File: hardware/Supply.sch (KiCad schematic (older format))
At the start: 11 parts, among them IC8 TL7702B, J1 Power, SW1 RESET, U1 R-785.0-0.5

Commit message: Working on layout
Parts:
- added D13: POWER, LED_THT:LED_D5.0mm, symbol Device:LED
- added R8: 470, Resistor_THT:R_Axial_DIN0207_L6.3mm_D2.5mm_P7.62mm_Horizontal, symbol Device:R
- C10, C11, C12, C13: footprint Capacitor_THT:C_Rect_L4.6mm_W2.0mm_P2.50mm_MKS02_FKP02 -> Capacitor_THT:C_Rect_L4.0mm_W2.5mm_P2.50mm; Mfr. AVX -> TDK; Mfr. No. SR295E104MAATR2 -> FA18X8R1H104KRU06; Mouser 581-SR295E104MAATR2 -> 810-FA18X8R1H104KRU6
- IC8: value TL7702B -> TL7702
- J1: value Power -> 12V
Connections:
- wire segments 33 -> 38
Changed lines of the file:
@@
 EESchema Schematic File Version 4
-LIBS:Sweet 6502 Computer-cache
+LIBS:Retro PC-cache
 EELAYER 30 0
 EELAYER END
@@
 F 1 "10k" H 5720 3605 50  0000 L CNN
 F 2 "Resistor_THT:R_Axial_DIN0207_L6.3mm_D2.5mm_P7.62mm_Horizontal" V 5580 3650 50  0001 C CNN
-F 3 "~" H 5650 3650 50  0001 C CNN
+F 3 "https://www.mouser.de/datasheet/2/427/sfr16s25-239894.pdf" H 5650 3650 50  0001 C CNN
 F 4 "Vishay / BC Components" H 5650 3650 50  0001 C CNN "Mfr."
 F 5 "SFR25H0001002JR500" H 5650 3650 50  0001 C CNN "Mfr. No."
@@
 F 0 "C11" H 6215 4446 50  0000 L CNN
 F 1 "100nF" H 6215 4355 50  0000 L CNN
-F 2 "Capacitor_THT:C_Rect_L4.6mm_W2.0mm_P2.50mm_MKS02_FKP02" H 6138 4250 50  0001 C CNN
-F 3 "~" H 6100 4400 50  0001 C CNN
-F 4 "AVX" H 6100 4400 50  0001 C CNN "Mfr."
-F 5 "SR295E104MAATR2" H 6100 4400 50  0001 C CNN "Mfr. No."
-F 6 "581-SR295E104MAATR2" H 6100 4400 50  0001 C CNN "Mouser"
+F 2 "Capacitor_THT:C_Rect_L4.0mm_W2.5mm_P2.50mm" H 6138 4250 50  0001 C CNN
+F 3 "https://www.mouser.de/datasheet/2/400/eadmlcc_halogenfree_fa150_en-890480.pdf" H 6100 4400 50  0001 C CNN
+F 4 "TDK" H 6100 4400 50  0001 C CNN "Mfr."
+F 5 "FA18X8R1H104KRU06" H 6100 4400 50  0001 C CNN "Mfr. No."
+F 6 "810-FA18X8R1H104KRU6" H 6100 4400 50  0001 C CNN "Mouser"
 	1    6100 4400
 	1    0    0    -1
@@
 F 1 "330nF" H 3365 4155 50  0000 L CNN
 F 2 "Capacitor_THT:C_Rect_L4.0mm_W2.5mm_P2.50mm" H 3288 4050 50  0001 C CNN
-F 3 "~" H 3250 4200 50  0001 C CNN
+F 3 "https://www.mouser.de/datasheet/2/40/SR-Series-1016911.pdf" H 3250 4200 50  0001 C CNN
 F 4 "AVX" H 3250 4200 50  0001 C CNN "Mfr."
 F 5 "SR205E334MARTR1" H 3250 4200 50  0001 C CNN "Mfr. No."
@@
 F 0 "C10" H 4315 4246 50  0000 L CNN
 F 1 "100nF" H 4315 4155 50  0000 L CNN
-F 2 "Capacitor_THT:C_Rect_L4.6mm_W2.0mm_P2.50mm_MKS02_FKP02" H 4238 4050 50  0001 C CNN
-F 3 "~" H 4200 4200 50  0001 C CNN
-F 4 "AVX" H 4200 4200 50  0001 C CNN "Mfr."
-F 5 "SR295E104MAATR2" H 4200 4200 50  0001 C CNN "Mfr. No."
-F 6 "581-SR295E104MAATR2" H 4200 4200 50  0001 C CNN "Mouser"
+F 2 "Capacitor_THT:C_Rect_L4.0mm_W2.5mm_P2.50mm" H 4238 4050 50  0001 C CNN
+F 3 "https://www.mouser.de/datasheet/2/400/eadmlcc_halogenfree_fa150_en-890480.pdf" H 4200 4200 50  0001 C CNN
+F 4 "TDK" H 4200 4200 50  0001 C CNN "Mfr."
+F 5 "FA18X8R1H104KRU06" H 4200 4200 50  0001 C CNN "Mfr. No."
+F 6 "810-FA18X8R1H104KRU6" H 4200 4200 50  0001 C CNN "Mouser"
 	1    4200 4200
 	1    0    0    -1
@@
 $EndComp
 Wire Wire Line
-	4200 3300 4200 3750
+	4200 3300 4200 3400
 Wire Wire Line
 	3450 3750 3250 3750
@@
 F 1 "1N4148" H 3000 3624 50  0000 C CNN
 F 2 "Diode_THT:D_DO-35_SOD27_P7.62mm_Horizontal" H 3000 3575 50  0001 C CNN
-F 3 "https://www.vishay.com/docs/81857/1n4148.pdf" H 3000 3750 50  0001 C CNN
+F 3 "https://www.mouser.de/datasheet/2/308/1N4148-1118184.pdf" H 3000 3750 50  0001 C CNN
 F 4 "ON Semiconductor / Fairchild" H 3000 3750 50  0001 C CNN "Mfr."
 F 5 "1N4148" H 3000 3750 50  0001 C CNN "Mfr. No."
@@
 AR Path="/5E9728CC/5E9AA4C9" Ref="J1"  Part="1"
 F 0 "J1" H 2457 4175 50  0000 C CNN
-F 1 "Power" H 2457 4084 50  0000 C CNN
+F 1 "12V" H 2457 4084 50  0000 C CNN
 F 2 "Connector_BarrelJack:BarrelJack_Wuerth_6941xx301002" H 2450 3810 50  0001 C CNN
 F 3 "https://katalog.we-online.de/em/datasheet/6941xx301002.pdf" H 2450 3810 50  0001 C CNN
@@
 F 0 "C12" H 6715 4446 50  0000 L CNN
 F 1 "100nF" H 6715 4355 50  0000 L CNN
-F 2 "Capacitor_THT:C_Rect_L4.6mm_W2.0mm_P2.50mm_MKS02_FKP02" H 6638 4250 50  0001 C CNN
-F 3 "~" H 6600 4400 50  0001 C CNN
-F 4 "AVX" H 6600 4400 50  0001 C CNN "Mfr."
-F 5 "SR295E104MAATR2" H 6600 4400 50  0001 C CNN "Mfr. No."
-F 6 "581-SR295E104MAATR2" H 6600 4400 50  0001 C CNN "Mouser"
+F 2 "Capacitor_THT:C_Rect_L4.0mm_W2.5mm_P2.50mm" H 6638 4250 50  0001 C CNN
+F 3 "https://www.mouser.de/datasheet/2/400/eadmlcc_halogenfree_fa150_en-890480.pdf" H 6600 4400 50  0001 C CNN
+F 4 "TDK" H 6600 4400 50  0001 C CNN "Mfr."
+F 5 "FA18X8R1H104KRU06" H 6600 4400 50  0001 C CNN "Mfr. No."
+F 6 "810-FA18X8R1H104KRU6" H 6600 4400 50  0001 C CNN "Mouser"
 	1    6600 4400
 	1    0    0    -1
@@
 F 0 "C13" H 8015 4446 50  0000 L CNN
 F 1 "100nF" H 8015 4355 50  0001 L CNN
-F 2 "Capacitor_THT:C_Rect_L4.6mm_W2.0mm_P2.50mm_MKS02_FKP02" H 7938 4250 50  0001 C CNN
-F 3 "~" H 7900 4400 50  0001 C CNN
-F 4 "AVX" H 7900 4400 50  0001 C CNN "Mfr."
-F 5 "SR295E104MAATR2" H 7900 4400 50  0001 C CNN "Mfr. No."
-F 6 "581-SR295E104MAATR2" H 7900 4400 50  0001 C CNN "Mouser"
+F 2 "Capacitor_THT:C_Rect_L4.0mm_W2.5mm_P2.50mm" H 7938 4250 50  0001 C CNN
+F 3 "https://www.mouser.de/datasheet/2/400/eadmlcc_halogenfree_fa150_en-890480.pdf" H 7900 4400 50  0001 C CNN
+F 4 "TDK" H 7900 4400 50  0001 C CNN "Mfr."
+F 5 "FA18X8R1H104KRU06" H 7900 4400 50  0001 C CNN "Mfr. No."
+F 6 "810-FA18X8R1H104KRU6" H 7900 4400 50  0001 C CNN "Mouser"
 	1    7900 4400
 	1    0    0    -1
@@
 AR Path="/5E9728CC/5E9AA51D" Ref="IC8"  Part="1"
 F 0 "IC8" H 6950 4350 50  0000 C CNN
-F 1 "TL7702B" H 7050 3650 50  0000 C CNN
+F 1 "TL7702" H 7050 3650 50  0000 C CNN
 F 2 "Package_DIP:DIP-8_W7.62mm_LongPads" H 7300 4000 50  0001 C CNN
 F 3 "http://www.ti.com.cn/cn/lit/ds/symlink/tl7705b.pdf" H 7300 4000 50  0001 C CNN
@@
 Wire Wire Line
 	2750 3950 2750 4650
+$Comp
+L Device:LED D?
+U 1 1 5D9EA3B0
+P 4750 4350
+AR Path="/5D9EA3B0" Ref="D?"  Part="1"
+AR Path="/5EB09E21/5D9EA3B0" Ref="D?"  Part="1"
+AR Path="/5EC67F7B/5D9EA3B0" Ref="D?"  Part="1"
+AR Path="/5E9728CC/5D9EA3B0" Ref="D13"  Part="1"
+F 0 "D13" V 4800 4200 50  0000 R CNN
+F 1 "POWER" V 4700 4200 50  0000 R CNN
+F 2 "LED_THT:LED_D5.0mm" H 4750 4350 50  0001 C CNN
+F 3 "https://www.mouser.de/datasheet/2/90/C503B_RAS_RAN_AAS_AAN_RBS_RBN_ABS_ABN_RCS_RCN_ACS_-269115.pdf" H 4750 4350 50  0001 C CNN
+F 4 "Cree Inc." H 4750 4350 50  0001 C CNN "Mfr."
+F 5 "C503B-RAN-CZ0C0AA1" H 4750 4350 50  0001 C CNN "Mfr. No."
+F 6 "941-C503BRANCZ0C0AA1" H 4750 4350 50  0001 C CNN "Mouser"
+	1    4750 4350
+	0    -1   -1   0
+$EndComp
+$Comp
+L Device:R R?
+U 1 1 5D9EA844
+P 4750 3850
+AR Path="/5D9EA844" Ref="R?"  Part="1"
+AR Path="/5E9728CC/5D9EA844" Ref="R8"  Part="1"
+F 0 "R8" H 4820 3896 50  0000 L CNN
+F 1 "470" H 4820 3805 50  0000 L CNN
+F 2 "Resistor_THT:R_Axial_DIN0207_L6.3mm_D2.5mm_P7.62mm_Horizontal" V 4680 3850 50  0001 C CNN
+F 3 "" H 4750 3850 50  0001 C CNN
+	1    4750 3850
+	1    0    0    -1
+$EndComp
+Wire Wire Line
+	4200 3400 4750 3400
+Wire Wire Line
+	4750 3400 4750 3700
+Connection ~ 4200 3400
+Wire Wire Line
+	4200 3400 4200 3750
+Wire Wire Line
+	4750 4000 4750 4200
+$Comp
+L power:GND #PWR?
+U 1 1 5D9EC35B
+P 4750 4650
+AR Path="/5D9EC35B" Ref="#PWR?"  Part="1"
+AR Path="/5E9728CC/5D9EC35B" Ref="#PWR056"  Part="1"
+F 0 "#PWR056" H 4750 4400 50  0001 C CNN
+F 1 "GND" H 4755 4477 50  0000 C CNN
+F 2 "" H 4750 4650 50  0001 C CNN
+F 3 "" H 4750 4650 50  0001 C CNN
+	1    4750 4650
+	1    0    0    -1
+$EndComp
+Wire Wire Line
+	4750 4650 4750 4500
 $EndSCHEMATC

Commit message: Working on layout
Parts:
- J1: footprint Connector_BarrelJack:BarrelJack_Wuerth_6941xx301002 -> Wuerth:BarrelJack_Wuerth_6941xx301002
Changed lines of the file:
@@
 $Descr A4 11693 8268
 encoding utf-8
-Sheet 3 6
+Sheet 2 6
 Title "Retro PC"
 Date "2019-10-08"
@@
 F 0 "J1" H 2457 4175 50  0000 C CNN
 F 1 "12V" H 2457 4084 50  0000 C CNN
-F 2 "Connector_BarrelJack:BarrelJack_Wuerth_6941xx301002" H 2450 3810 50  0001 C CNN
+F 2 "Wuerth:BarrelJack_Wuerth_6941xx301002" H 2450 3810 50  0001 C CNN
 F 3 "https://katalog.we-online.de/em/datasheet/6941xx301002.pdf" H 2450 3810 50  0001 C CNN
 F 4 "Wurth Elektronik" H 2400 3850 50  0001 C CNN "Mfr."

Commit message: Working on layout
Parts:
- removed J1: 12V, Wuerth:BarrelJack_Wuerth_6941xx301002, symbol Connector:Barrel_Jack
- added X1: ConBarrel, Wuerth:BarrelJack_Wuerth_6941xx301002, symbol Wuerth:ConBarrel
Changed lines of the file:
@@
 	3750 4050 3750 4650
-$Comp
-L Connector:Barrel_Jack J?
-U 1 1 5E9AA4C9
-P 2400 3850
-AR Path="/5E9AA4C9" Ref="J?"  Part="1"
-AR Path="/5E9728CC/5E9AA4C9" Ref="J1"  Part="1"
-F 0 "J1" H 2457 4175 50  0000 C CNN
-F 1 "12V" H 2457 4084 50  0000 C CNN
-F 2 "Wuerth:BarrelJack_Wuerth_6941xx301002" H 2450 3810 50  0001 C CNN
-F 3 "https://katalog.we-online.de/em/datasheet/6941xx301002.pdf" H 2450 3810 50  0001 C CNN
-F 4 "Wurth Elektronik" H 2400 3850 50  0001 C CNN "Mfr."
-F 5 "694106301002" H 2400 3850 50  0001 C CNN "Mfr. No."
-F 6 "710-694106301002" H 2400 3850 50  0001 C CNN "Mouser"
-	1    2400 3850
-	1    0    0    -1
-$EndComp
 $Comp
 L power:GND #PWR?
@@
 Wire Wire Line
 	4750 4650 4750 4500
+$Comp
+L Wuerth:ConBarrel X1
+U 1 1 5DA7C8DA
+P 2400 3850
+F 0 "X1" H 2457 4083 50  0000 C CNN
+F 1 "ConBarrel" H 2400 3650 50  0001 C CNN
+F 2 "Wuerth:BarrelJack_Wuerth_6941xx301002" H 2450 3810 50  0001 C CNN
+F 3 "https://katalog.we-online.de/em/datasheet/6941xx301002.pdf" H 2450 3810 50  0001 C CNN
+F 4 "Wurth Elektronik" H 2400 3850 50  0001 C CNN "Mfr."
+F 5 "694106301002" H 2400 3850 50  0001 C CNN "Mfr. No."
+F 6 "710-694106301002" H 2400 3850 50  0001 C CNN "Mouser"
+	1    2400 3850
+	1    0    0    -1
+$EndComp
 $EndSCHEMATC

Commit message: Working on layout
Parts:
- U1: Mfr. No. R-785.0-0.5 -> R-785.0-1.0; Mouser 919-R-785.0-0.5 -> 919-R-785.0-1.0
- X1: value ConBarrel -> DC IN; footprint Wuerth:BarrelJack_Wuerth_6941xx301002 -> Connector_Custom:BarrelJack_Wuerth_6941xx301002
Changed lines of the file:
@@
 F 2 "Converter_DCDC:Converter_DCDC_RECOM_R-78E-0.5_THT" H 3800 3500 50  0001 L CIN
 F 3 "https://www.recom-power.com/pdf/Innoline/R-78xx-0.5.pdf" H 3750 3750 50  0001 C CNN
-F 4 "919-R-785.0-0.5" H 3750 3750 50  0001 C CNN "Mouser"
-F 5 "R-785.0-0.5" H 3750 3750 50  0001 C CNN "Mfr. No."
+F 4 "919-R-785.0-1.0" H 3750 3750 50  0001 C CNN "Mouser"
+F 5 "R-785.0-1.0" H 3750 3750 50  0001 C CNN "Mfr. No."
 F 6 "Recom" H 3750 3750 50  0001 C CNN "Mfr."
 	1    3750 3750
@@
 P 2400 3850
 F 0 "X1" H 2457 4083 50  0000 C CNN
-F 1 "ConBarrel" H 2400 3650 50  0001 C CNN
-F 2 "Wuerth:BarrelJack_Wuerth_6941xx301002" H 2450 3810 50  0001 C CNN
+F 1 "DC IN" H 2400 3650 50  0000 C CNN
+F 2 "Connector_Custom:BarrelJack_Wuerth_6941xx301002" H 2450 3810 50  0001 C CNN
 F 3 "https://katalog.we-online.de/em/datasheet/6941xx301002.pdf" H 2450 3810 50  0001 C CNN
 F 4 "Wurth Elektronik" H 2400 3850 50  0001 C CNN "Mfr."

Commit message: First version of the layout
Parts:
- R5: Mfr. Vishay / BC Components -> Yageo; Mfr. No. SFR25H0001002JR500 -> MFP-25BRD52-10K; Mouser 594-SFR25H0001002JR5 -> 603-MFP-25BRD52-10K
- R8: Mfr. (none) -> Yageo; Mfr. No. (none) -> MFP-25BRD52-470R; Mouser (none) -> 603-MFP-25BRD52-470R
- U1: value R-785.0-0.5 -> R-785.0-1.0; symbol Regulator_Switching:R-785.0-0.5 -> Regulator_Switching:R-785.0-1.0
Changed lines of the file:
@@
 F 1 "10k" H 5720 3605 50  0000 L CNN
 F 2 "Resistor_THT:R_Axial_DIN0207_L6.3mm_D2.5mm_P7.62mm_Horizontal" V 5580 3650 50  0001 C CNN
-F 3 "https://www.mouser.de/datasheet/2/427/sfr16s25-239894.pdf" H 5650 3650 50  0001 C CNN
-F 4 "Vishay / BC Components" H 5650 3650 50  0001 C CNN "Mfr."
-F 5 "SFR25H0001002JR500" H 5650 3650 50  0001 C CNN "Mfr. No."
-F 6 "594-SFR25H0001002JR5" H 5650 3650 50  0001 C CNN "Mouser"
+F 3 "https://www.mouser.de/datasheet/2/447/Yageo%20LR_MFP_2013-594635.pdf" H 5650 3650 50  0001 C CNN
+F 4 "Yageo" H 5650 3650 50  0001 C CNN "Mfr."
+F 5 "MFP-25BRD52-10K" H 5650 3650 50  0001 C CNN "Mfr. No."
+F 6 "603-MFP-25BRD52-10K" H 5650 3650 50  0001 C CNN "Mouser"
 	1    5650 3650
 	1    0    0    -1
@@
 	2700 3750 2850 3750
 $Comp
-L Regulator_Switching:R-785.0-0.5 U?
+L Regulator_Switching:R-785.0-1.0 U?
 U 1 1 5E9AA4DB
 P 3750 3750
@@
 AR Path="/5E9728CC/5E9AA4DB" Ref="U1"  Part="1"
 F 0 "U1" H 3750 3992 50  0000 C CNN
-F 1 "R-785.0-0.5" H 3750 3901 50  0000 C CNN
+F 1 "R-785.0-1.0" H 3750 3901 50  0000 C CNN
 F 2 "Converter_DCDC:Converter_DCDC_RECOM_R-78E-0.5_THT" H 3800 3500 50  0001 L CIN
-F 3 "https://www.recom-power.com/pdf/Innoline/R-78xx-0.5.pdf" H 3750 3750 50  0001 C CNN
+F 3 "https://www.recom-power.com/pdf/Innoline/R-78xx-0.1.pdf" H 3750 3750 50  0001 C CNN
 F 4 "919-R-785.0-1.0" H 3750 3750 50  0001 C CNN "Mouser"
 F 5 "R-785.0-1.0" H 3750 3750 50  0001 C CNN "Mfr. No."
@@
 F 1 "470" H 4820 3805 50  0000 L CNN
 F 2 "Resistor_THT:R_Axial_DIN0207_L6.3mm_D2.5mm_P7.62mm_Horizontal" V 4680 3850 50  0001 C CNN
-F 3 "" H 4750 3850 50  0001 C CNN
+F 3 "https://www.mouser.de/datasheet/2/447/Yageo%20LR_MFP_2013-594635.pdf" H 4750 3850 50  0001 C CNN
+F 4 "Yageo" H 4750 3850 50  0001 C CNN "Mfr."
+F 5 "MFP-25BRD52-470R" H 4750 3850 50  0001 C CNN "Mfr. No."
+F 6 "603-MFP-25BRD52-470R" H 4750 3850 50  0001 C CNN "Mouser"
 	1    4750 3850
 	1    0    0    -1

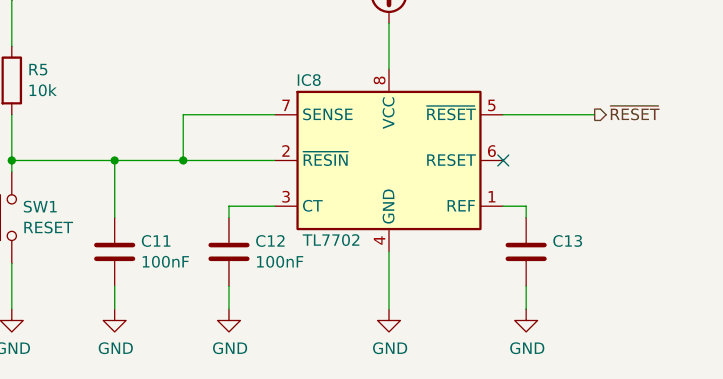
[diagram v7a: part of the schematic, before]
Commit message: Finalize schematic and layout. Add switch for carrier detect
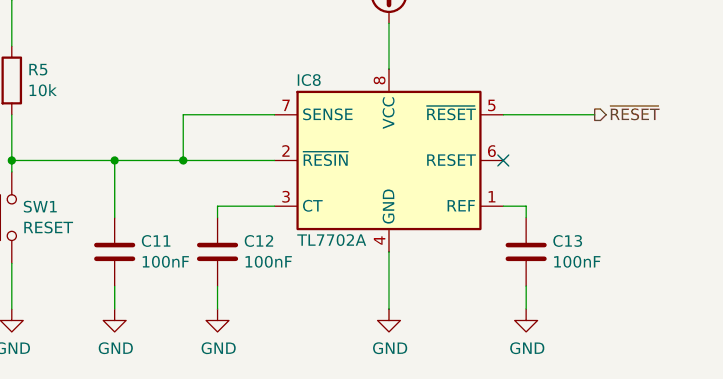
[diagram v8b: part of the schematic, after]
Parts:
- IC8: value TL7702 -> TL7702A
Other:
- moved on the sheet: C12
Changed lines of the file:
@@
 Date "2019-10-08"
 Rev "1.0"
-Comp ""
+Comp "https://www.kampis-elektroecke.de"
 Comment1 "Author: Daniel Kampert"
 Comment2 ""
@@
 L Device:C C?
 U 1 1 5E9AA4F6
-P 6600 4400
+P 6550 4400
 AR Path="/5E9AA4F6" Ref="C?"  Part="1"
 AR Path="/5E9728CC/5E9AA4F6" Ref="C12"  Part="1"
-F 0 "C12" H 6715 4446 50  0000 L CNN
-F 1 "100nF" H 6715 4355 50  0000 L CNN
-F 2 "Capacitor_THT:C_Rect_L4.0mm_W2.5mm_P2.50mm" H 6638 4250 50  0001 C CNN
-F 3 "https://www.mouser.de/datasheet/2/400/eadmlcc_halogenfree_fa150_en-890480.pdf" H 6600 4400 50  0001 C CNN
-F 4 "TDK" H 6600 4400 50  0001 C CNN "Mfr."
-F 5 "FA18X8R1H104KRU06" H 6600 4400 50  0001 C CNN "Mfr. No."
-F 6 "810-FA18X8R1H104KRU6" H 6600 4400 50  0001 C CNN "Mouser"
-	1    6600 4400
+F 0 "C12" H 6665 4446 50  0000 L CNN
+F 1 "100nF" H 6665 4355 50  0000 L CNN
+F 2 "Capacitor_THT:C_Rect_L4.0mm_W2.5mm_P2.50mm" H 6588 4250 50  0001 C CNN
+F 3 "https://www.mouser.de/datasheet/2/400/eadmlcc_halogenfree_fa150_en-890480.pdf" H 6550 4400 50  0001 C CNN
+F 4 "TDK" H 6550 4400 50  0001 C CNN "Mfr."
+F 5 "FA18X8R1H104KRU06" H 6550 4400 50  0001 C CNN "Mfr. No."
+F 6 "810-FA18X8R1H104KRU6" H 6550 4400 50  0001 C CNN "Mouser"
+	1    6550 4400
 	1    0    0    -1
 $EndComp
@@
 L power:GND #PWR?
 U 1 1 5E9AA4FC
-P 6600 4650
+P 6550 4650
 AR Path="/5E9AA4FC" Ref="#PWR?"  Part="1"
 AR Path="/5E9728CC/5E9AA4FC" Ref="#PWR043"  Part="1"
-F 0 "#PWR043" H 6600 4400 50  0001 C CNN
-F 1 "GND" H 6605 4477 50  0000 C CNN
-F 2 "" H 6600 4650 50  0001 C CNN
-F 3 "" H 6600 4650 50  0001 C CNN
-	1    6600 4650
-	1    0    0    -1
-$EndComp
-Wire Wire Line
-	6600 4550 6600 4650
-Wire Wire Line
-	6800 4200 6600 4200
-Wire Wire Line
-	6600 4200 6600 4250
+F 0 "#PWR043" H 6550 4400 50  0001 C CNN
+F 1 "GND" H 6555 4477 50  0000 C CNN
+F 2 "" H 6550 4650 50  0001 C CNN
+F 3 "" H 6550 4650 50  0001 C CNN
+	1    6550 4650
+	1    0    0    -1
+$EndComp
+Wire Wire Line
+	6550 4550 6550 4650
+Wire Wire Line
+	6800 4200 6550 4200
+Wire Wire Line
+	6550 4200 6550 4250
 $Comp
 L Device:C C?
@@
 AR Path="/5E9728CC/5E9AA505" Ref="C13"  Part="1"
 F 0 "C13" H 8015 4446 50  0000 L CNN
-F 1 "100nF" H 8015 4355 50  0001 L CNN
+F 1 "100nF" H 8015 4355 50  0000 L CNN
 F 2 "Capacitor_THT:C_Rect_L4.0mm_W2.5mm_P2.50mm" H 7938 4250 50  0001 C CNN
 F 3 "https://www.mouser.de/datasheet/2/400/eadmlcc_halogenfree_fa150_en-890480.pdf" H 7900 4400 50  0001 C CNN
@@
 AR Path="/5E9728CC/5E9AA51D" Ref="IC8"  Part="1"
 F 0 "IC8" H 6950 4350 50  0000 C CNN
-F 1 "TL7702" H 7050 3650 50  0000 C CNN
+F 1 "TL7702A" H 7050 3650 50  0000 C CNN
 F 2 "Package_DIP:DIP-8_W7.62mm_LongPads" H 7300 4000 50  0001 C CNN
 F 3 "http://www.ti.com.cn/cn/lit/ds/symlink/tl7705b.pdf" H 7300 4000 50  0001 C CNN
